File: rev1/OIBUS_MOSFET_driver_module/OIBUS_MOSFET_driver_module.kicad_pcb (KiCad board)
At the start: 2 copper layers, 90.2 x 95.9 mm, 152 parts, among them J1 SWD, J10 +, J11 +, J12 +, J13 +, J2 UART, J3 5V - 24V, Molex Ultrafit, J4 +, J5 +, J6 +, J7 +, J8 +, J9 +, T1 DMG6402LVT, T10 DMG6402LVT, T2 DMG6402LVT, T3 DMG6402LVT, T4 DMG6402LVT, T5 DMG6402LVT, T6 DMG6402LVT, T7 DMG6402LVT, T8 DMG6402LVT, T9 DMG6402LVT, U1 TLP291, U10 STM32F303CCTx, U11 TLP291, U12 TLP291, U2 TLP291, U3 TLP291, U4 TLP291, U5 TLP291, U6 TLP291, U7 TLP291, U8 TLP291, U9 TCAN330, Y1 16M

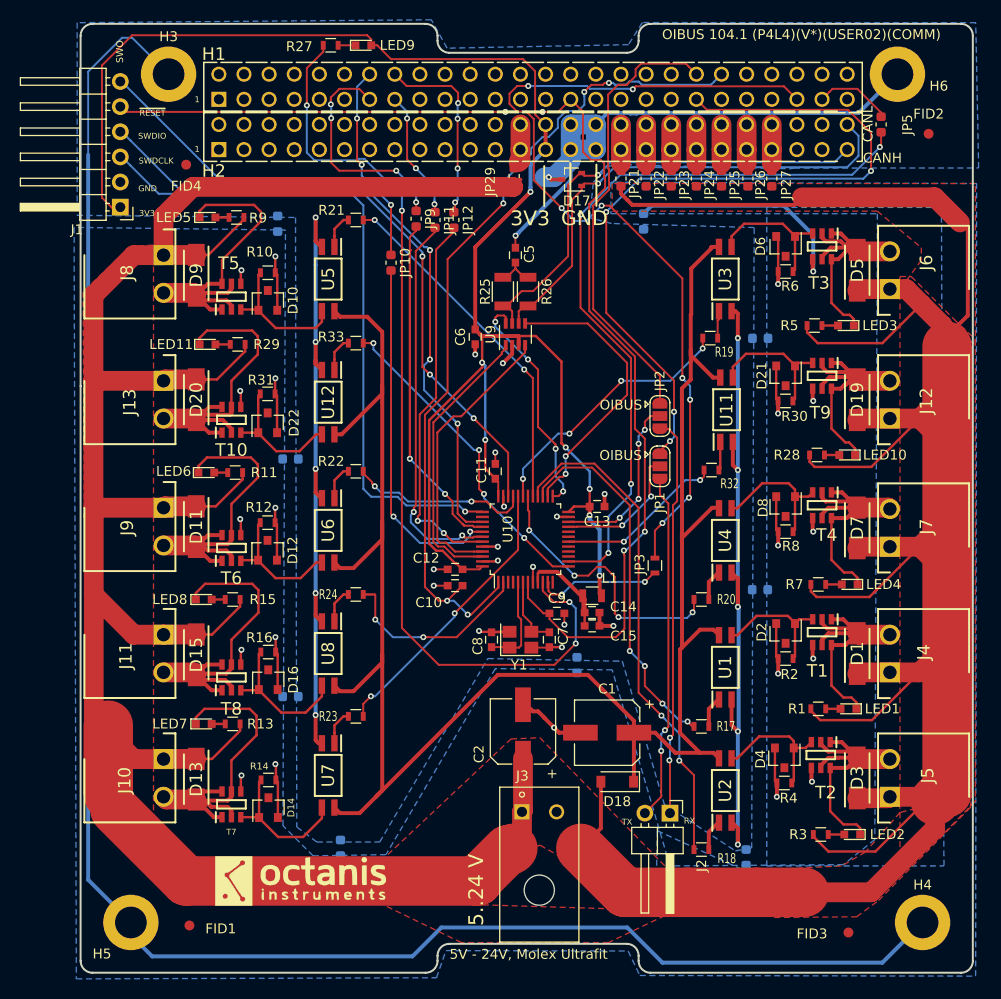
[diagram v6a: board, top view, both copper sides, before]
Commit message: fixing zener footprint, rotating leds for side view, added uavcan micro connector
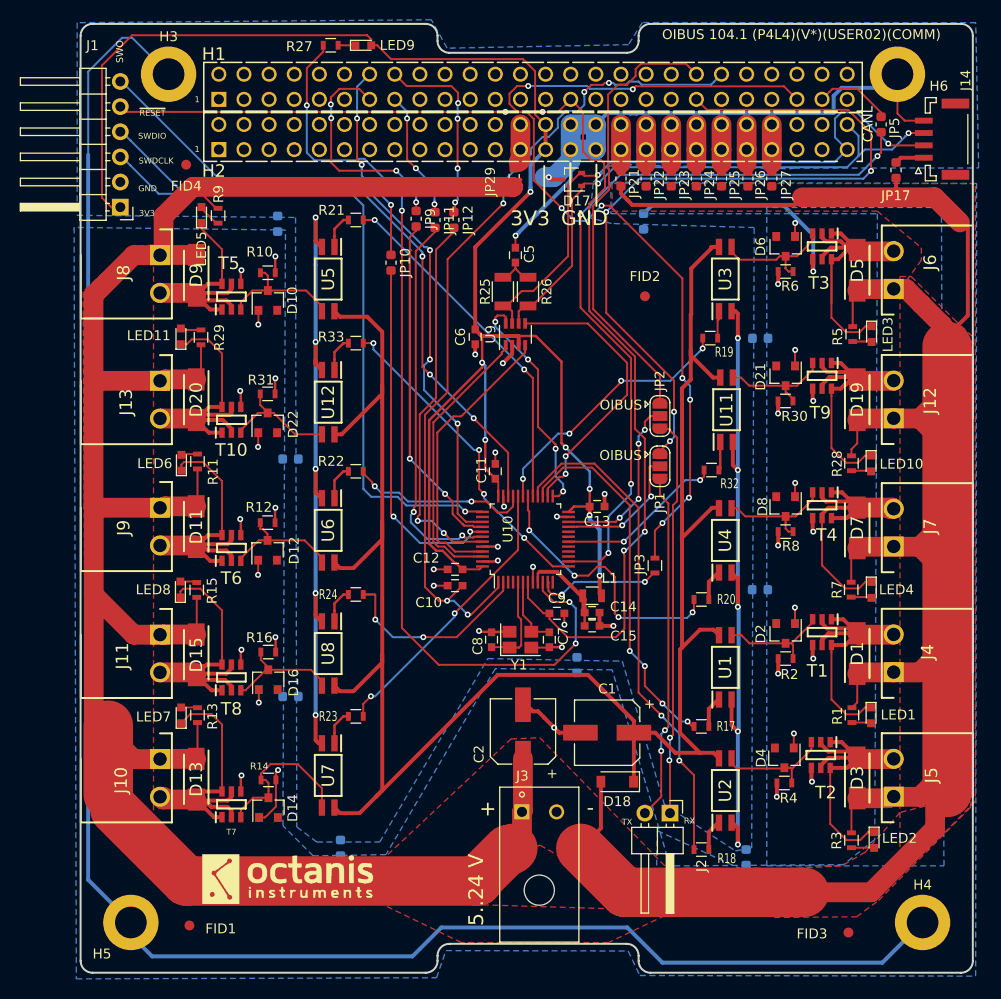
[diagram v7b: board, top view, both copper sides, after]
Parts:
- added J14: UAVCAN JST GH, Connectors_JST:JST_GH_SM04B-GHS-TB_04x1.25mm_Angled, F.Cu at (135.2, 54.7)
- added JP17: 0 OHM, Resistor_SMD:R_0603_1608Metric, F.Cu at (130.8, 57.8)
- D10, D12, D14, D16, D2, D21, D22, D4, D6, D8: footprint TO_SOT_Packages_SMD:SOT-23 -> Diodes_SMD:D_SOT-23_ANK
- moved FID2 33.0 mm to (105.4, 70.6)
- moved R11 3.97 mm to (60.2, 87.3), turned to 270 degrees
- moved R5 3.96 mm to (126.4, 74.4), turned to 90 degrees
- moved R29 3.78 mm to (60.6, 74.7), turned to 270 degrees
- moved R15 3.76 mm to (60.1, 100.3), turned to 270 degrees
- moved R13 3.67 mm to (60.2, 112.9), turned to 270 degrees
- moved R28 3.58 mm to (126.3, 87.5), turned to 90 degrees
- moved R1 3.46 mm to (126.3, 112.9), turned to 90 degrees
- moved R7 3.37 mm to (126.3, 100.2), turned to 90 degrees
- moved R3 3.15 mm to (126.3, 125.6), turned to 90 degrees
- moved LED11 2.81 mm to (58.5, 74.6), turned to 90 degrees
- moved LED3 2.73 mm to (128.3, 74.4), turned to 270 degrees
- moved LED6 2.70 mm to (58.6, 87.4), turned to 90 degrees
- moved LED8 2.57 mm to (58.5, 100.2), turned to 90 degrees
- moved LED10 2.56 mm to (128.3, 87.5), turned to 270 degrees
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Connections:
- H1 pad 1: Net-(H1-Pad1) -> (no net)
- H1 pad 10: Net-(H1-Pad10) -> (no net)
- H1 pad 11: Net-(H1-Pad11) -> (no net)
- H1 pad 12: Net-(H1-Pad12) -> (no net)
- H1 pad 17: Net-(H1-Pad17) -> (no net)
- H1 pad 18: Net-(H1-Pad18) -> (no net)
- H1 pad 19: Net-(H1-Pad19) -> (no net)
- H1 pad 2: Net-(H1-Pad2) -> (no net)
- H1 pad 20: Net-(H1-Pad20) -> (no net)
- H1 pad 21: Net-(H1-Pad21) -> (no net)
- H1 pad 22: Net-(H1-Pad22) -> (no net)
- H1 pad 23: Net-(H1-Pad23) -> (no net)
- H1 pad 24: Net-(H1-Pad24) -> (no net)
- H1 pad 25: Net-(H1-Pad25) -> (no net)
- H1 pad 26: Net-(H1-Pad26) -> (no net)
- H1 pad 27: Net-(H1-Pad27) -> (no net)
- H1 pad 28: Net-(H1-Pad28) -> (no net)
- H1 pad 3: Net-(H1-Pad3) -> (no net)
- H1 pad 30: Net-(H1-Pad30) -> (no net)
- H1 pad 31: Net-(H1-Pad31) -> (no net)
- H1 pad 32: Net-(H1-Pad32) -> (no net)
- H1 pad 33: Net-(H1-Pad33) -> (no net)
- H1 pad 34: Net-(H1-Pad34) -> (no net)
- H1 pad 35: Net-(H1-Pad35) -> (no net)
- H1 pad 36: Net-(H1-Pad36) -> (no net)
- H1 pad 37: Net-(H1-Pad37) -> (no net)
- H1 pad 38: Net-(H1-Pad38) -> (no net)
- H1 pad 4: Net-(H1-Pad4) -> (no net)
- H1 pad 41: Net-(H1-Pad41) -> (no net)
- H1 pad 43: Net-(H1-Pad43) -> (no net)
- H1 pad 44: Net-(H1-Pad44) -> (no net)
- H1 pad 45: Net-(H1-Pad45) -> (no net)
- H1 pad 46: Net-(H1-Pad46) -> (no net)
- H1 pad 48: Net-(H1-Pad48) -> (no net)
- H1 pad 5: Net-(H1-Pad5) -> (no net)
- H1 pad 50: Net-(H1-Pad50) -> (no net)
- H1 pad 51: Net-(H1-Pad51) -> (no net)
- H1 pad 52: Net-(H1-Pad52) -> (no net)
- H1 pad 6: Net-(H1-Pad6) -> (no net)
- H1 pad 7: Net-(H1-Pad7) -> (no net)
- H1 pad 8: Net-(H1-Pad8) -> (no net)
- H1 pad 9: Net-(H1-Pad9) -> (no net)
- H2 pad 1: Net-(H2-Pad1) -> (no net)
- H2 pad 10: Net-(H2-Pad10) -> (no net)
- H2 pad 11: Net-(H2-Pad11) -> (no net)
- H2 pad 12: Net-(H2-Pad12) -> (no net)
- H2 pad 13: Net-(H2-Pad13) -> (no net)
- H2 pad 14: Net-(H2-Pad14) -> (no net)
- H2 pad 15: Net-(H2-Pad15) -> (no net)
- H2 pad 16: Net-(H2-Pad16) -> (no net)
- H2 pad 17: Net-(H2-Pad17) -> (no net)
- H2 pad 18: Net-(H2-Pad18) -> (no net)
- H2 pad 19: Net-(H2-Pad19) -> (no net)
- H2 pad 2: Net-(H2-Pad2) -> (no net)
- H2 pad 20: Net-(H2-Pad20) -> (no net)
- H2 pad 21: Net-(H2-Pad21) -> (no net)
- H2 pad 22: Net-(H2-Pad22) -> (no net)
- H2 pad 23: Net-(H2-Pad23) -> (no net)
- H2 pad 24: Net-(H2-Pad24) -> (no net)
- H2 pad 3: Net-(H2-Pad3) -> (no net)
- H2 pad 4: Net-(H2-Pad4) -> (no net)
- H2 pad 47: Net-(H2-Pad47) -> (no net)
- H2 pad 48: Net-(H2-Pad48) -> (no net)
- H2 pad 49: Net-(H2-Pad49) -> (no net)
- H2 pad 5: Net-(H2-Pad5) -> (no net)
- H2 pad 50: Net-(H2-Pad50) -> (no net)
- H2 pad 6: Net-(H2-Pad6) -> (no net)
- H2 pad 7: Net-(H2-Pad7) -> (no net)
- H2 pad 8: Net-(H2-Pad8) -> (no net)
- H2 pad 9: Net-(H2-Pad9) -> (no net)
- U10 pad 12: Net-(U10-Pad12) -> (no net)
- U10 pad 15: Net-(U10-Pad15) -> (no net)
- U10 pad 16: Net-(U10-Pad16) -> (no net)
- U10 pad 17: Net-(U10-Pad17) -> (no net)
- U10 pad 19: Net-(U10-Pad19) -> (no net)
- U10 pad 20: Net-(U10-Pad20) -> (no net)
- U10 pad 3: Net-(U10-Pad3) -> (no net)
- U10 pad 38: Net-(U10-Pad38) -> (no net)
- U10 pad 4: Net-(U10-Pad4) -> (no net)
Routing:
- net VBUS: track 546.3 -> 479.4 mm
- net GNDPWR: track 96.4 -> 76.2 mm, vias 21 -> 30
- net CANH: track 47.5 -> 61.8 mm, vias 1 -> 2
- net Net-(D9-Pad2): track 34.5 -> 25.6 mm
- net GND: track 404.3 -> 412.2 mm
- net CANL: track 49.9 -> 57.5 mm, vias 1 -> 2
- net Net-(D15-Pad2): track 34.7 -> 30.0 mm
- net Net-(D20-Pad2): track 33.8 -> 29.2 mm
- net Net-(D11-Pad2): track 34.4 -> 30.3 mm
- net Net-(D13-Pad2): track 35.1 -> 31.4 mm
- net Net-(D7-Pad2): track 26.7 -> 30.1 mm
- net Net-(D19-Pad2): track 26.4 -> 29.8 mm
- net Net-(D5-Pad2): track 25.7 -> 28.9 mm
- net Net-(J14-Pad1): track 0.00 -> 3.00 mm
- net Net-(D1-Pad2): track 26.4 -> 29.2 mm
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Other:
- board text added: "+"
- board text added: "-"
- board text added: "OIBUS MOSFET driver (10 ch) Rev 1b, 2019, SS Octanis Instruments OÜ www.octanis.ch"
- board text removed: "CANH"
- board text removed: "OIBUS MOSFET driver (10 ch) Rev 1, 2018, SS Octanis Instruments OÜ www.octanis.ch"

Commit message: adding disclaimer
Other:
- board text added: "For prototyping purposes only, not approved for resale."
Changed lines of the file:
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@@
   (general
     (thickness 1.6)
-    (drawings 48)
+    (drawings 49)
     (tracks 1641)
     (zones 0)
@@
       (xy -4.8895 2.50825)) (layer F.SilkS) (width 0.01))
   )
+  (gr_text "For prototyping purposes only, not approved for resale." (at 94.234 58.6486) (layer B.SilkS)
+    (effects (font (size 1.5 1.5) (thickness 0.3)))
+  )
   (gr_text - (at 99.8982 122.2502) (layer F.SilkS)
